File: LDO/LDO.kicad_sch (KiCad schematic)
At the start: 4 parts, among them U1801 L78L05_SOT89

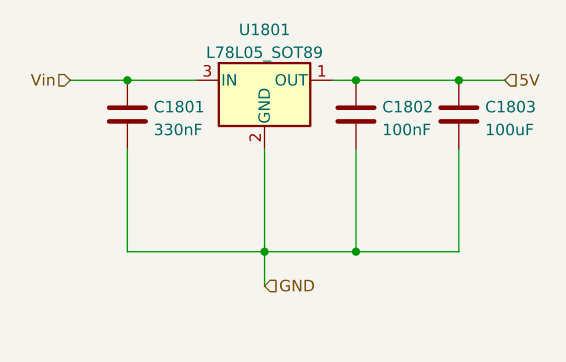
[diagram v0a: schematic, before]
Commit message: added 12V boost converter (300mA max!)
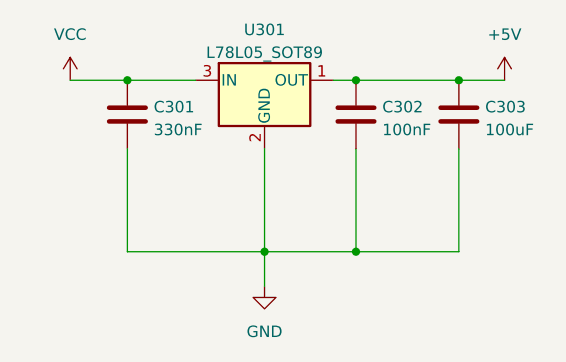
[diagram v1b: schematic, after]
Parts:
- renumbered C1801 to C301, C1802 to C302, C1803 to C303, U1801 to U301
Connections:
- net 5V renamed +5V
- net Vin renamed VCC
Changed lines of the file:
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@@
     (stroke (width 0) (type default))
   )
-  (hierarchical_label "GND" (shape input) (at 193.04 111.76 0) (fields_autoplaced)
-    (effects (font (size 1.27 1.27)) (justify left))
-  )
-  (hierarchical_label "Vin" (shape input) (at 171.45 88.9 180) (fields_autoplaced)
-    (effects (font (size 1.27 1.27)) (justify right))
-  )
-  (hierarchical_label "5V" (shape input) (at 219.71 88.9 0) (fields_autoplaced)
-    (effects (font (size 1.27 1.27)) (justify left))
+  (symbol (lib_id "power:GND") (at 193.04 111.76 0) (unit 1)
+    (in_bom yes) (on_board yes) (dnp no) (fields_autoplaced)
+    (property "Reference" "#PWR0102" (at 193.04 118.11 0)
+      (effects (font (size 1.27 1.27)) hide)
+    )
+    (property "Value" "GND" (at 193.04 116.84 0)
+      (effects (font (size 1.27 1.27)))
+    )
+    (property "Footprint" "" (at 193.04 111.76 0)
+      (effects (font (size 1.27 1.27)) hide)
+    )
+    (property "Datasheet" "" (at 193.04 111.76 0)
+      (effects (font (size 1.27 1.27)) hide)
+    )
+    (pin "1")
+    (instances
+      (project "LDO"
+        (path "/81bbecec-1528-4fdb-9ae5-dd524e2ba32e"
+          (reference "#PWR0102") (unit 1)
+        )
+      )
+    )
   )
   (symbol (lib_id "Device:C") (at 203.2 92.71 0) (unit 1)
     (in_bom yes) (on_board yes) (dnp no) (fields_autoplaced)
-    (property "Reference" "C1802" (at 206.121 91.8753 0)
+    (property "Reference" "C302" (at 206.121 91.8753 0)
       (effects (font (size 1.27 1.27)) (justify left))
     )
@@
   (symbol (lib_id "Regulator_Linear:L78L05_SOT89") (at 193.04 88.9 0) (unit 1)
     (in_bom yes) (on_board yes) (dnp no) (fields_autoplaced)
-    (property "Reference" "U1801" (at 193.04 83.2952 0)
+    (property "Reference" "U301" (at 193.04 83.2952 0)
       (effects (font (size 1.27 1.27)))
     )
@@
     )
   )
+  (symbol (lib_id "power:VCC") (at 171.45 88.9 0) (unit 1)
+    (in_bom yes) (on_board yes) (dnp no) (fields_autoplaced)
+    (property "Reference" "#PWR0103" (at 171.45 92.71 0)
+      (effects (font (size 1.27 1.27)) hide)
+    )
+    (property "Value" "VCC" (at 171.45 83.82 0)
+      (effects (font (size 1.27 1.27)))
+    )
+    (property "Footprint" "" (at 171.45 88.9 0)
+      (effects (font (size 1.27 1.27)) hide)
+    )
+    (property "Datasheet" "" (at 171.45 88.9 0)
+      (effects (font (size 1.27 1.27)) hide)
+    )
+    (pin "1")
+    (instances
+      (project "LDO"
+        (path "/81bbecec-1528-4fdb-9ae5-dd524e2ba32e"
+          (reference "#PWR0103") (unit 1)
+        )
+      )
+    )
+  )
+  (symbol (lib_id "power:+5V") (at 219.71 88.9 0) (unit 1)
+    (in_bom yes) (on_board yes) (dnp no) (fields_autoplaced)
+    (property "Reference" "#PWR0101" (at 219.71 92.71 0)
+      (effects (font (size 1.27 1.27)) hide)
+    )
+    (property "Value" "+5V" (at 219.71 83.82 0)
+      (effects (font (size 1.27 1.27)))
+    )
+    (property "Footprint" "" (at 219.71 88.9 0)
+      (effects (font (size 1.27 1.27)) hide)
+    )
+    (property "Datasheet" "" (at 219.71 88.9 0)
+      (effects (font (size 1.27 1.27)) hide)
+    )
+    (pin "1")
+    (instances
+      (project "LDO"
+        (path "/81bbecec-1528-4fdb-9ae5-dd524e2ba32e"
+          (reference "#PWR0101") (unit 1)
+        )
+      )
+    )
+  )
   (symbol (lib_id "Device:C") (at 177.8 92.71 0) (unit 1)
     (in_bom yes) (on_board yes) (dnp no) (fields_autoplaced)
-    (property "Reference" "C1801" (at 180.721 91.8753 0)
+    (property "Reference" "C301" (at 180.721 91.8753 0)
       (effects (font (size 1.27 1.27)) (justify left))
     )
@@
   (symbol (lib_id "Device:C") (at 214.63 92.71 0) (unit 1)
     (in_bom yes) (on_board yes) (dnp no) (fields_autoplaced)
-    (property "Reference" "C1803" (at 217.551 91.8753 0)
+    (property "Reference" "C303" (at 217.551 91.8753 0)
       (effects (font (size 1.27 1.27)) (justify left))
     )
